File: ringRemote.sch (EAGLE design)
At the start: 13 parts, among them Y1 32.768kHz

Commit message: added a todo list; did some thinking for the HMI pushbuttons
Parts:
- added R1, R4, R5, R6: 100k, ringRemote:RESISTOR
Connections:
- new net 3.3V: R1.2, R4.2, R5.2, R6.2
- new net N$6: R4.1, U$1.SWDIOALT
- new net N$7: R1.1, U$1.SWDCLKALT
- new net N$8: R5.1, U$1.P0.3
- new net N$9: R6.1, U$1.P0.2
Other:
- note added: "not adding a sch part, but there are hypothetical switches here. will probably create some vias with some conductive filament under (as carrier) then pot with conductive glue"
- moved on the sheet: C1, C2, C3, C4, C5, C6, D1, R2, R3, U$1, U$2, Y1

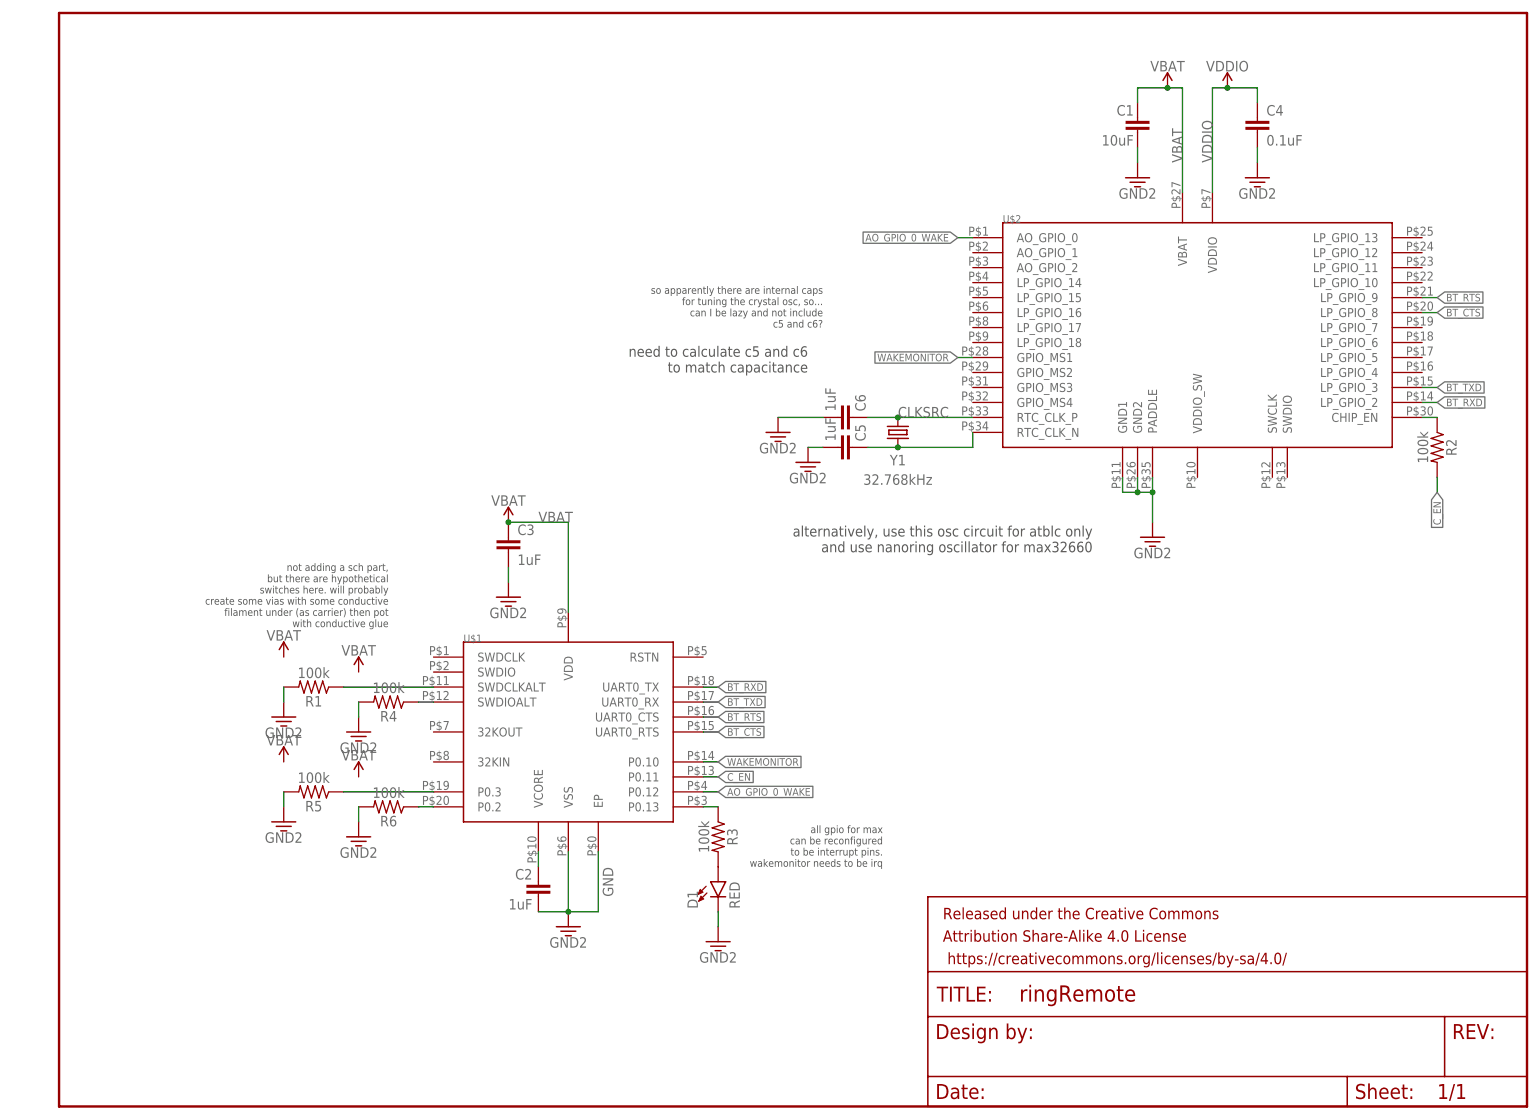
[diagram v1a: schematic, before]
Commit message: added to bom: battery supervisor, charging circuit components; put components on board space to estimate stuff
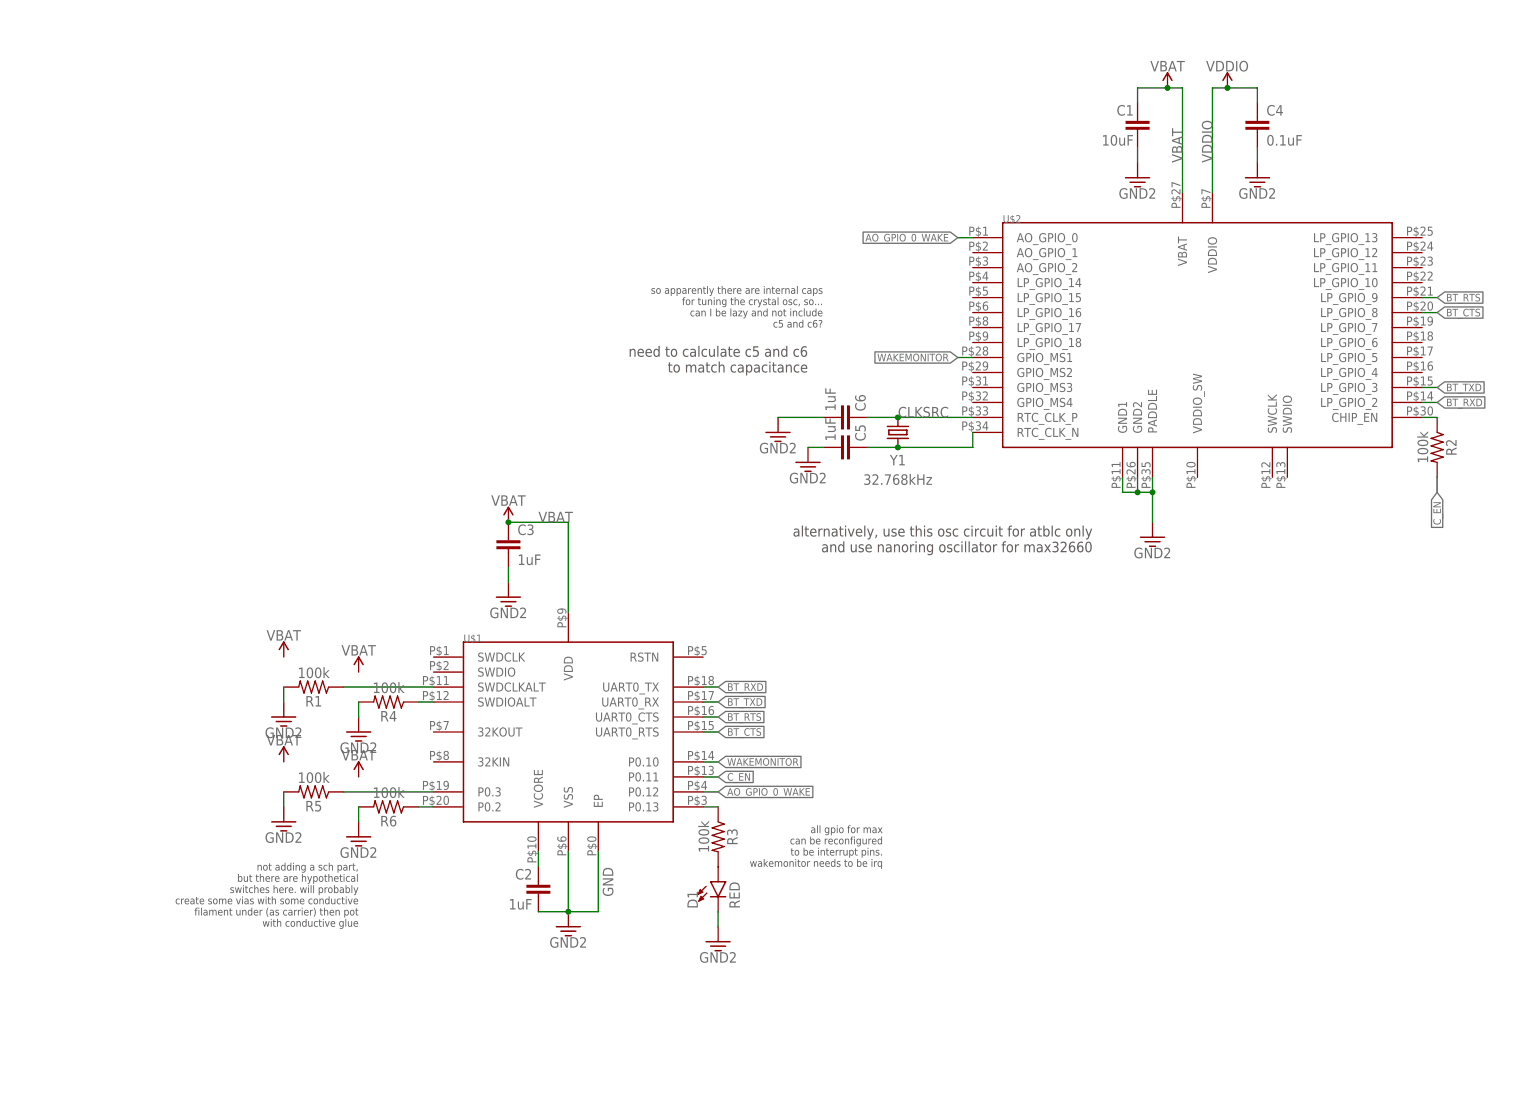
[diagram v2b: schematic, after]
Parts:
- removed FRAME1: FRAME-LETTER, SparkFun-Aesthetics:FRAME-LETTER
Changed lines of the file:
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@@
 </classes>
 <parts>
-<part name="FRAME1" library="SparkFun-Aesthetics" deviceset="FRAME-LETTER" device=""/>
 <part name="D1" library="ringRemote" deviceset="LED" device="0603" value="RED"/>
 <part name="Y1" library="ringRemote" deviceset="CRYSTAL-32.768KHZ" device="SMD-3.2X1.5" value="32.768kHz"/>
@@
 can I be lazy and not include
 c5 and c6?</text>
-<text x="55.88" y="81.28" size="1.27" layer="97" align="bottom-right">not adding a sch part,
+<text x="50.8" y="30.48" size="1.27" layer="97" align="bottom-right">not adding a sch part,
 but there are hypothetical
 switches here. will probably
@@
 </plain>
 <instances>
-<instance part="FRAME1" gate="G$1" x="0" y="0"/>
-<instance part="FRAME1" gate="V" x="147.32" y="0"/>
 <instance part="D1" gate="G$1" x="111.76" y="38.1"/>
 <instance part="Y1" gate="G$1" x="142.24" y="114.3" smashed="yes" rot="R270">

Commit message: added battery supervisor part, wired it up
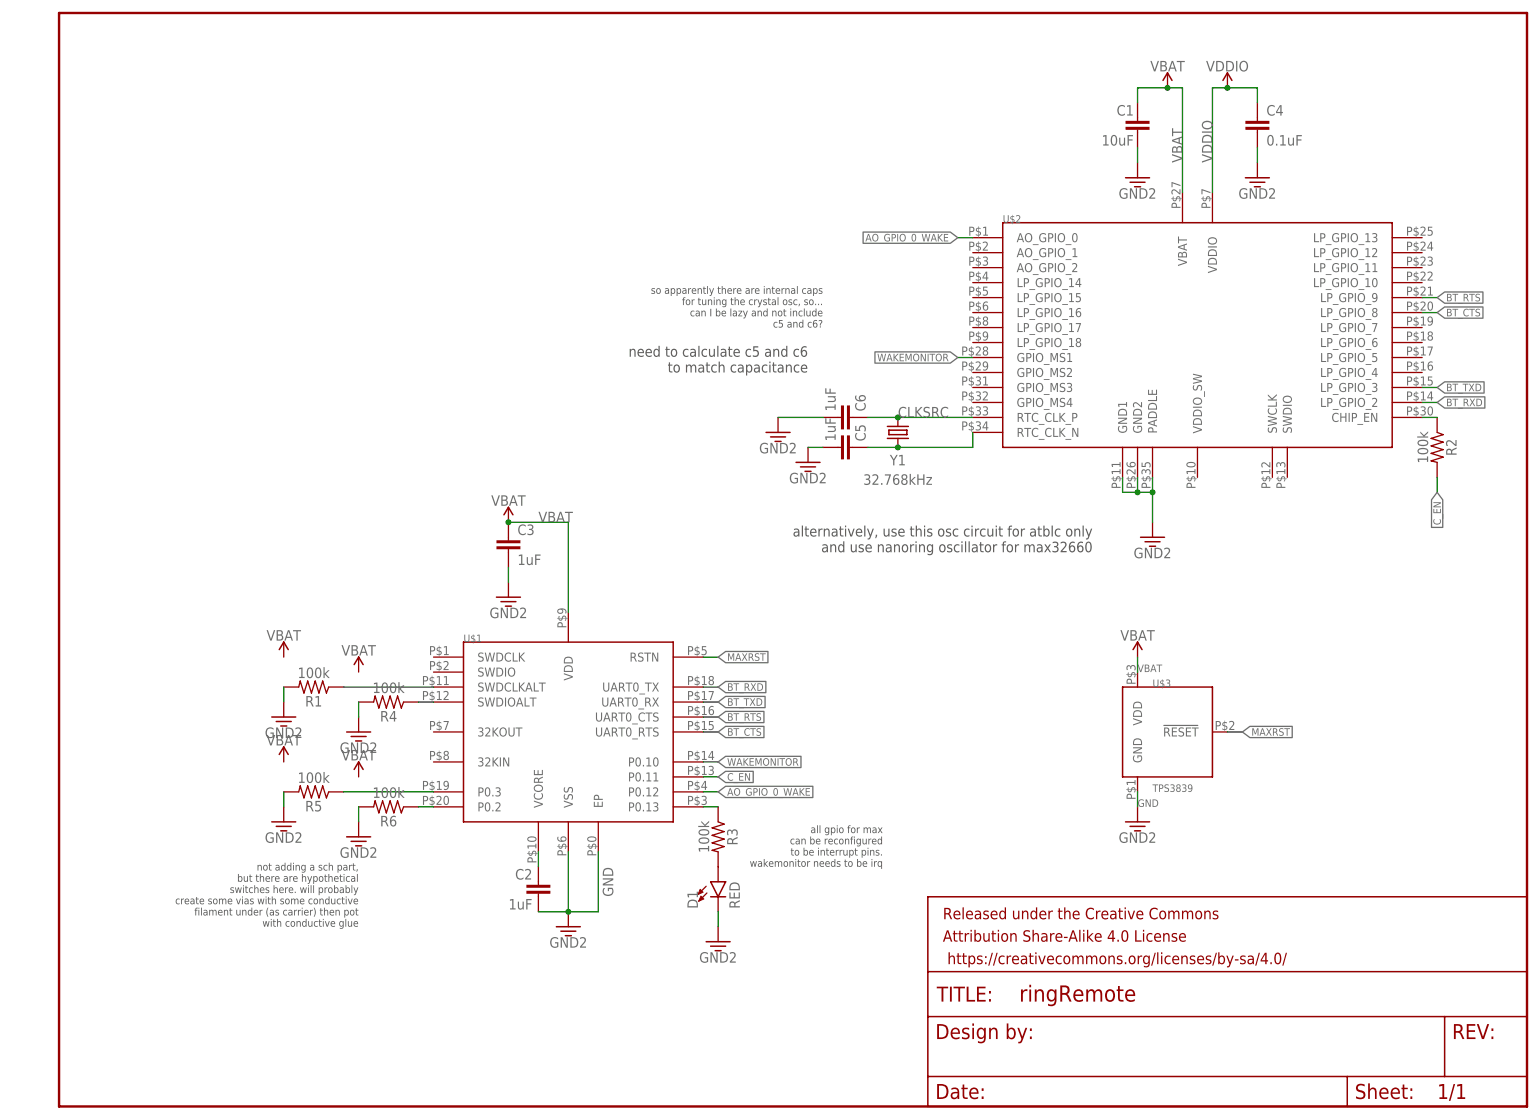
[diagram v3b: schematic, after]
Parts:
- added FRAME1: FRAME-LETTERNO_PACKAGE, SparkFun-Aesthetics:FRAME-LETTERNO_PACKAGE
- added U$3: TPS3839, ringRemote:TPS3839
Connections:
- removed net 3.3V: R1.2, R4.2, R5.2, R6.2
- new net MAXRST: U$1.RSTN, U$3.!RESET
- net GND: now also R1.2, R4.2, R5.2, R6.2, U$3.GND
- net VBAT: now also U$3.VDD
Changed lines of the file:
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@@
 <part name="SUPPLY6" library="SparkFun-PowerSymbols" deviceset="VCC" device="" value="VBAT"/>
 <part name="SUPPLY7" library="SparkFun-PowerSymbols" deviceset="VCC" device="" value="VBAT"/>
+<part name="U$3" library="ringRemote" deviceset="TPS3839" device=""/>
+<part name="SUPPLY8" library="SparkFun-PowerSymbols" deviceset="VCC" device="" value="VBAT"/>
+<part name="GND13" library="SparkFun-PowerSymbols" deviceset="GND2" device=""/>
+<part name="FRAME1" library="SparkFun-Aesthetics" deviceset="FRAME-LETTER" device="NO_PACKAGE"/>
 </parts>
 <sheets>
@@
 <instance part="SUPPLY6" gate="G$1" x="38.1" y="58.42"/>
 <instance part="SUPPLY7" gate="G$1" x="50.8" y="55.88"/>
+<instance part="U$3" gate="G$1" x="187.96" y="63.5"/>
+<instance part="SUPPLY8" gate="G$1" x="182.88" y="76.2"/>
+<instance part="GND13" gate="G$1" x="182.88" y="48.26"/>
+<instance part="FRAME1" gate="G$1" x="0" y="0"/>
+<instance part="FRAME1" gate="V" x="147.32" y="0"/>
 </instances>
 <busses>
@@
 <wire x1="111.76" y1="30.48" x2="111.76" y2="33.02" width="0.1524" layer="91"/>
 </segment>
+<segment>
+<pinref part="R6" gate="G$1" pin="2"/>
+<pinref part="GND3" gate="G$1" pin="3.3V"/>
+<wire x1="50.8" y1="50.8" x2="50.8" y2="48.26" width="0.1524" layer="91"/>
+</segment>
+<segment>
+<pinref part="R5" gate="G$1" pin="2"/>
+<pinref part="GND10" gate="G$1" pin="3.3V"/>
+<wire x1="38.1" y1="53.34" x2="38.1" y2="50.8" width="0.1524" layer="91"/>
+</segment>
+<segment>
+<pinref part="R1" gate="G$1" pin="2"/>
+<pinref part="GND11" gate="G$1" pin="3.3V"/>
+<wire x1="38.1" y1="71.12" x2="38.1" y2="68.58" width="0.1524" layer="91"/>
+</segment>
+<segment>
+<pinref part="R4" gate="G$1" pin="2"/>
+<pinref part="GND12" gate="G$1" pin="3.3V"/>
+<wire x1="50.8" y1="68.58" x2="50.8" y2="66.04" width="0.1524" layer="91"/>
+</segment>
+<segment>
+<pinref part="U$3" gate="G$1" pin="GND"/>
+<wire x1="182.88" y1="53.34" x2="182.88" y2="50.8" width="0.1524" layer="91"/>
+<pinref part="GND13" gate="G$1" pin="3.3V"/>
+<label x="182.88" y="50.8" size="1.27" layer="95"/>
+</segment>
 </net>
 <net name="N$4" class="0">
@@
 <junction x="76.2" y="99.06"/>
 </segment>
+<segment>
+<pinref part="U$3" gate="G$1" pin="VDD"/>
+<wire x1="182.88" y1="73.66" x2="182.88" y2="76.2" width="0.1524" layer="91"/>
+<pinref part="SUPPLY8" gate="G$1" pin="VCC"/>
+<label x="182.88" y="73.66" size="1.27" layer="95"/>
+</segment>
 </net>
 <net name="VDDIO" class="0">
@@
 </segment>
 </net>
-<net name="3.3V" class="0">
-<segment>
-<pinref part="R6" gate="G$1" pin="2"/>
-<pinref part="GND3" gate="G$1" pin="3.3V"/>
-<wire x1="50.8" y1="50.8" x2="50.8" y2="48.26" width="0.1524" layer="91"/>
-</segment>
-<segment>
-<pinref part="R5" gate="G$1" pin="2"/>
-<pinref part="GND10" gate="G$1" pin="3.3V"/>
-<wire x1="38.1" y1="53.34" x2="38.1" y2="50.8" width="0.1524" layer="91"/>
-</segment>
-<segment>
-<pinref part="R1" gate="G$1" pin="2"/>
-<pinref part="GND11" gate="G$1" pin="3.3V"/>
-<wire x1="38.1" y1="71.12" x2="38.1" y2="68.58" width="0.1524" layer="91"/>
-</segment>
-<segment>
-<pinref part="R4" gate="G$1" pin="2"/>
-<pinref part="GND12" gate="G$1" pin="3.3V"/>
-<wire x1="50.8" y1="68.58" x2="50.8" y2="66.04" width="0.1524" layer="91"/>
-</segment>
-</net>
+<net name="MAXRST" class="0">
+<segment>
+<pinref part="U$1" gate="G$1" pin="RSTN"/>
+<wire x1="109.22" y1="76.2" x2="111.76" y2="76.2" width="0.1524" layer="91"/>
+<label x="111.76" y="76.2" size="1.27" layer="95" xref="yes"/>
+</segment>
+<segment>
+<pinref part="U$3" gate="G$1" pin="!RESET"/>
+<wire x1="198.12" y1="63.5" x2="200.66" y2="63.5" width="0.1524" layer="91"/>
+<label x="200.66" y="63.5" size="1.27" layer="95" xref="yes"/>
+</segment>
+</net>

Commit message: made a new sheet, moved all power stuff to second sheet; added charger circuit; added connector; added battery. pretty much just need to determine the programming interface before I start doing board layout
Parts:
- added C7: 1uF, ringRemote:CAPACITOR
- added D2: PANASONIC_DB2J31400LPANASONIC_DB2J31400L_0_0, ringRemote:PANASONIC_DB2J31400LPANASONIC_DB2J31400L_0_0
- added FRAME2: FRAME-LETTERNO_PACKAGE, SparkFun-Aesthetics:FRAME-LETTERNO_PACKAGE
- added J1: AMPHENOL_10118192-0001LFAMPHENOL_10118192-0001LF_0_0, ringRemote:AMPHENOL_10118192-0001LFAMPHENOL_10118192-0001LF_0_0
- added R7: 1.8k, ringRemote:RESISTOR0805
- added U$4: TLV700, ringRemote:TLV700
- added U$5: ML621S, ringRemote:ML621S
- U$3: value TPS3839 -> TPS3839G25
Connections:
- new net D+: J1.3
- new net D-: J1.2
- new net N$10: D2.ANODE, U$4.OUT
- new net VCC: C1.1, C3.1, D2.CATHODE, R7.2, U$1.VDD, U$2.VBAT, U$3.VDD
- new net VUSB: C7.1, J1.1, U$4.EN, U$4.IN
- net GND: now also C7.2, J1.5, J1.MNT_1, J1.MNT_2, J1.MNT_3, J1.MNT_4, J1.MNT_5, J1.MNT_6, U$4.GND, U$5.-
- net VBAT: now also R7.1, U$5.+; no longer C1.1, C3.1, U$1.VDD, U$2.VBAT, U$3.VDD
